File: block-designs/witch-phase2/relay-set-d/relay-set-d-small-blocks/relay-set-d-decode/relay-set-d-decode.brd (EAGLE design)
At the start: 99.1 x 78.7 mm, 85 parts, among them IC1 74LS138D, IC10 74LVC1G32DBV, IC11 74LVC1G32DBV, IC12 74LVC1G32DBV, IC13 74LVC1G125DBV, IC14 74LVC1G125DBV, IC15 74LVC1G125DBV, IC16 74LVC1G125DBV, IC17 74LVC1G125DBV, IC18 74LVC1G125DBV, IC19 74LVC1G125DBV, IC2 74LS138D, IC20 74LVC1G125DBV, IC21 74LVC1G125DBV, IC22 74LVC1G125DBV, IC23 74LVC1G125DBV, IC24 74LVC1G125DBV, IC25 74LVC1G04DBV, IC26 74LVC1G04DBV, IC3 74LS138D, IC4 74LS138D, IC5 74LVC1G32DBV, IC6 74LVC1G32DBV, IC7 74LVC1G32DBV, IC8 74LVC1G32DBV, IC9 74LVC1G32DBV

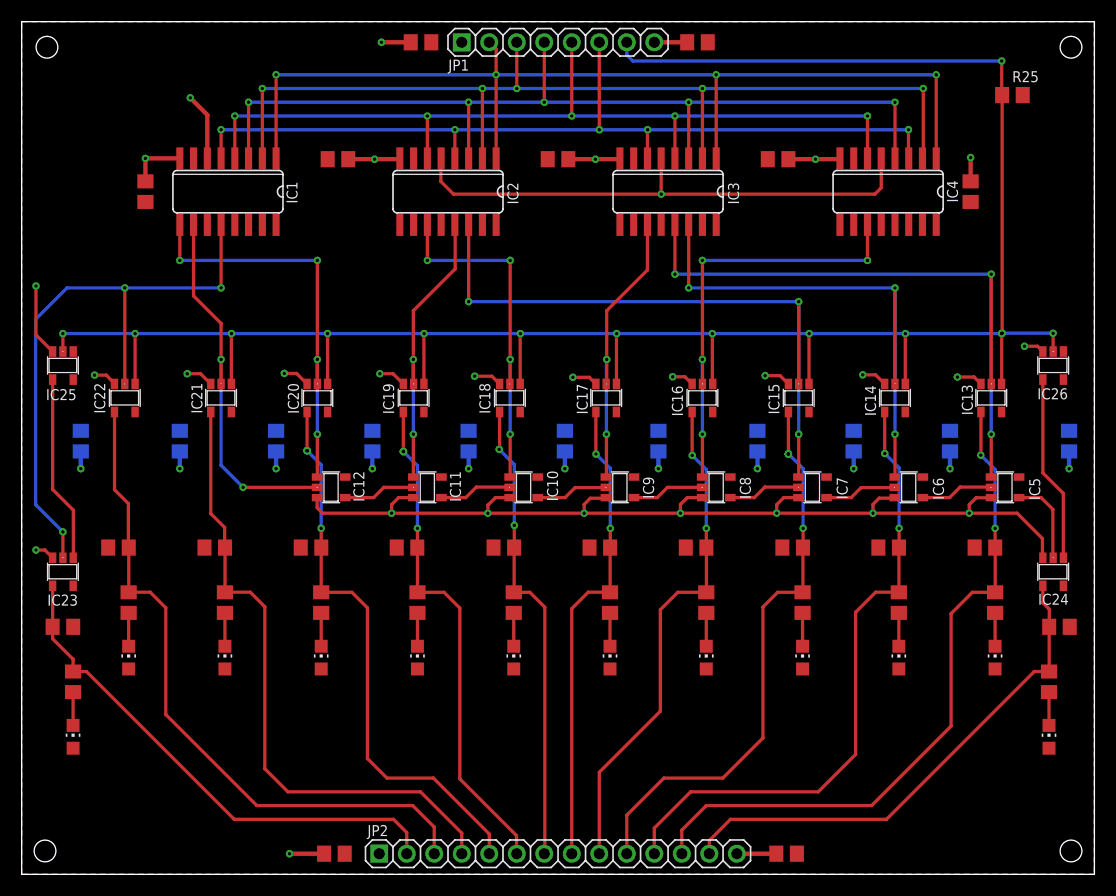
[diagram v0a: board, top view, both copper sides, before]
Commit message: adjust borders for ground/vcc plains and size to match 1.1inch grids
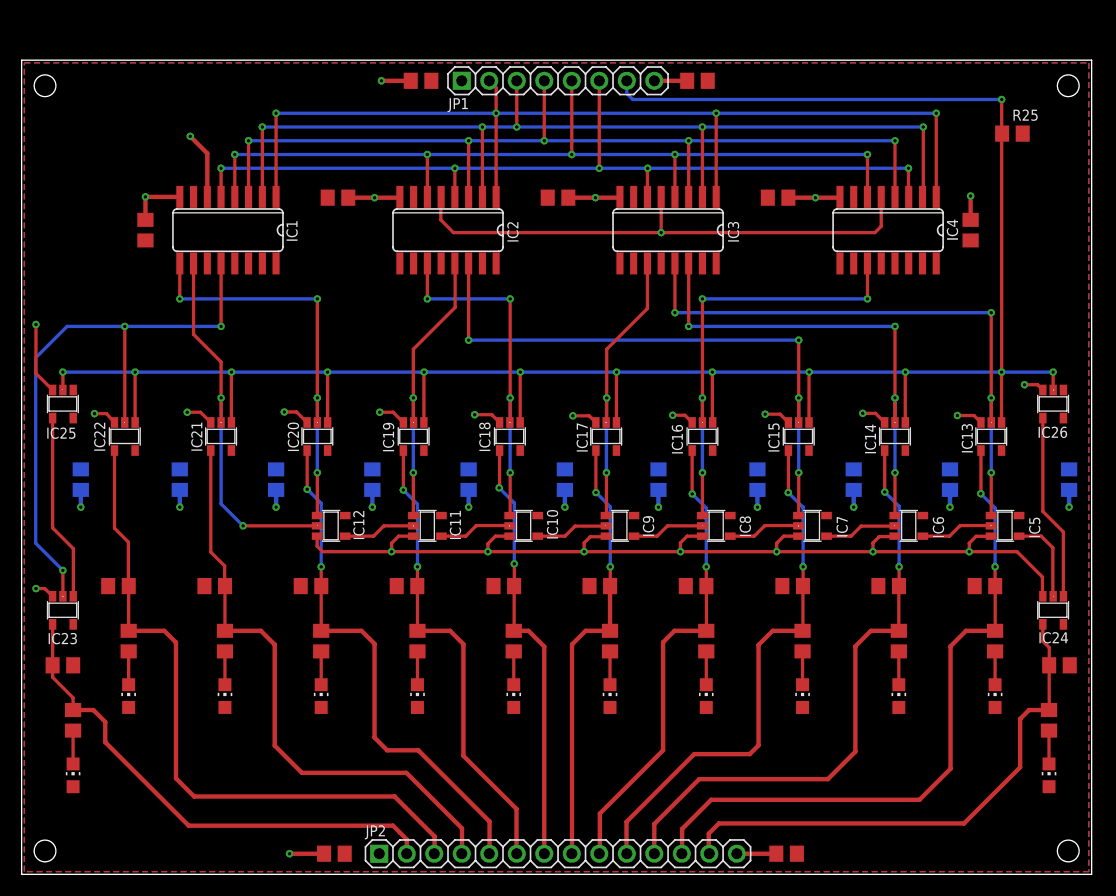
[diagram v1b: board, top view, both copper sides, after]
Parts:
- moved R25 3.56 mm to (91.5, 68.4)
- moved C1 3.56 mm to (29.2, 62.5)
- moved C10 3.56 mm to (67.9, 36.4)
- moved C12 3.56 mm to (76.8, 36.4)
- moved C13 3.56 mm to (5.46, 36.4)
- moved C14 3.56 mm to (85.7, 36.4)
- moved C15 3.56 mm to (14.6, 36.4)
- moved C16 3.56 mm to (96.7, 36.4)
- moved C17 3.56 mm to (23.5, 36.4)
- moved C18 3.56 mm to (32.4, 36.4)
- moved C20 3.56 mm to (41.3, 36.4)
- moved C3 3.56 mm to (49.5, 62.5)
- moved C4 3.56 mm to (69.8, 62.5)
- moved C6 3.56 mm to (50.2, 36.4)
- moved C8 3.56 mm to (58.8, 36.4)
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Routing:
- net NINE: track 62.6 -> 54.8 mm, vias 3 -> 4
- net EIGHT: track 51.2 -> 44.6 mm, vias 3 -> 4
- net SEVEN: track 61.4 -> 56.0 mm, vias 3 -> 4
- net ONE_N: track 58.9 -> 54.5 mm
- net TWO_N: track 52.0 -> 48.1 mm, vias 3 -> 2
- net FOUR_N: track 43.5 -> 39.8 mm
- net SEVEN_N: track 52.6 -> 49.2 mm, vias 3 -> 2
- net FIVE_N: track 44.0 -> 40.6 mm
- net SIX_N: track 47.0 -> 43.6 mm
- net EIGHT_N: track 59.4 -> 56.2 mm
- net THREE_N: track 46.6 -> 43.4 mm, vias 3 -> 2
- net !ONE-NINE_OUT: track 47.2 -> 48.8 mm
- net NINE_N: track 63.5 -> 62.6 mm
- net !ZERO_OUT: track 47.6 -> 46.9 mm
- net DSA-DSB: track 202.7 -> 202.6 mm, vias 14 -> 13
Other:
- board size 99.1 x 78.7 mm -> 98.8 x 75.2 mm

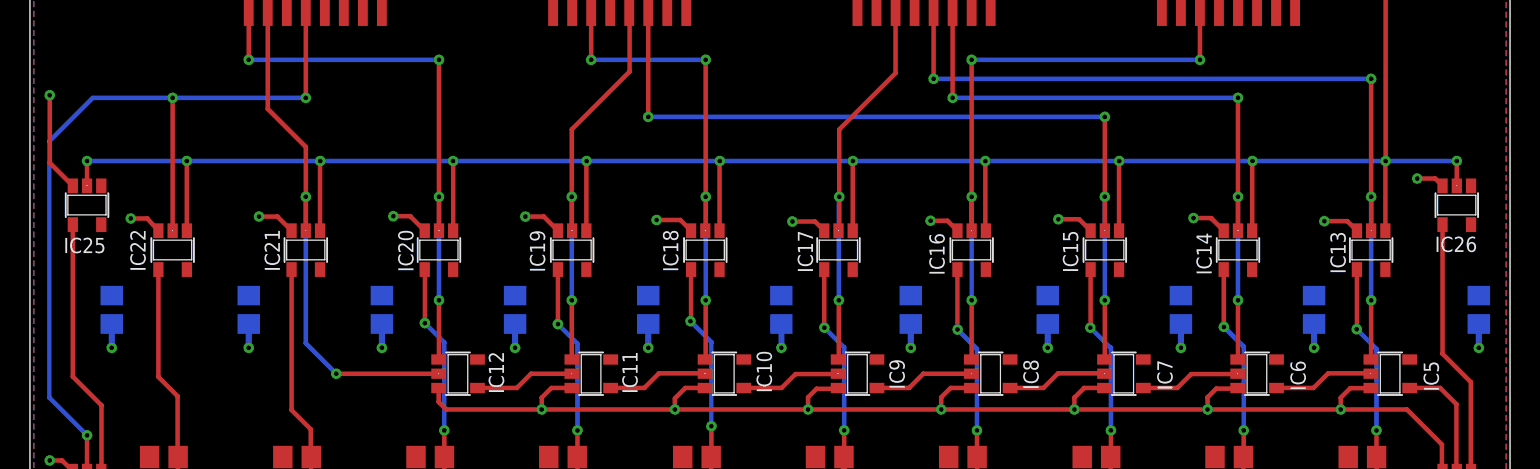
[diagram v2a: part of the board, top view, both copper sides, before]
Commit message: fixes for the decode - change OR gates to AND gates
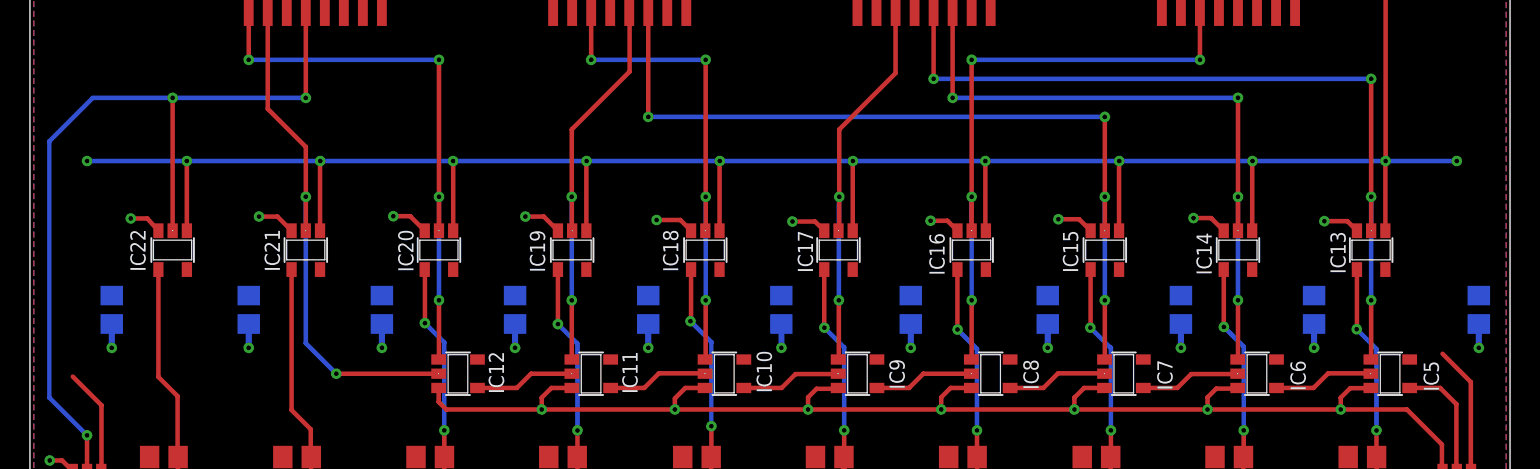
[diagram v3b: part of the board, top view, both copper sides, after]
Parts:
- removed IC25, IC26: 74LVC1G04DBV, 74xx-little-us:SOT23-5
- IC23, IC24: value 74LVC1G125DBV -> 74LVC1G126DBV
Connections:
- net !DSA-DSB-A: no longer IC25.4
- net !DSA-DSB-B: no longer IC26.4
- net DSA-DSB: no longer IC25.2, IC26.2
- net GND: no longer IC25.3, IC26.3
- net VCC: no longer IC25.5, IC26.5
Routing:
- net !DSA-DSB-A: track 17.3 -> 7.11 mm
- net !DSA-DSB-B: track 17.2 -> 8.63 mm
- net GND: track 211.6 -> 203.0 mm, vias 28 -> 26
- net DSA-DSB: track 202.6 -> 199.3 mm
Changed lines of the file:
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@@
 <layer number="43" name="vRestrict" color="2" fill="10" visible="no" active="yes"/>
 <layer number="44" name="Drills" color="7" fill="1" visible="no" active="yes"/>
-<layer number="45" name="Holes" color="7" fill="1" visible="yes" active="yes"/>
+<layer number="45" name="Holes" color="7" fill="1" visible="no" active="yes"/>
 <layer number="46" name="Milling" color="3" fill="1" visible="no" active="yes"/>
 <layer number="47" name="Measures" color="7" fill="1" visible="no" active="yes"/>
 <layer number="48" name="Document" color="7" fill="1" visible="yes" active="yes"/>
-<layer number="49" name="Reference" color="7" fill="1" visible="no" active="yes"/>
+<layer number="49" name="Reference" color="7" fill="1" visible="yes" active="yes"/>
 <layer number="50" name="dxf" color="7" fill="1" visible="no" active="no"/>
 <layer number="51" name="tDocu" color="7" fill="1" visible="yes" active="yes"/>
@@
 <circle x="2.159" y="2.159" radius="2.0066" width="0.0254" layer="41"/>
 <circle x="2.159" y="2.159" radius="2.0066" width="0.0254" layer="42"/>
-<text x="9.2456" y="12.7508" size="1.778" layer="51">0</text>
+<text x="9.2456" y="12.7508" size="1.778" layer="48">0</text>
 <text x="18.161" y="12.7508" size="1.778" layer="51">1</text>
 <text x="27.0002" y="12.7508" size="1.778" layer="51">2</text>
@@
 <text x="80.391" y="12.7508" size="1.778" layer="51">8</text>
 <text x="89.2556" y="12.7508" size="1.778" layer="51">9</text>
-<text x="93.091" y="5.4356" size="1.778" layer="51">1-9</text>
-<text x="4.0386" y="5.4356" size="1.778" layer="51">0</text>
-<text x="8.89" y="2.54" size="1.778" layer="51">Relay Set D
+<text x="93.091" y="5.4356" size="1.778" layer="48">1-9</text>
+<text x="4.0386" y="5.4356" size="1.778" layer="48">0</text>
+<text x="8.89" y="2.54" size="1.778" layer="48">Relay Set D
    Decode </text>
 </plain>
@@
 <attribute name="VALUE" x="89.5858" y="29.1592" size="1.27" layer="27" rot="R180"/>
 </element>
-<element name="IC24" library="74xx-little-us" package="SOT23-5" value="74LVC1G125DBV" x="95.25" y="24.384" smashed="yes" rot="R180">
+<element name="IC24" library="74xx-little-us" package="SOT23-5" value="74LVC1G126DBV" x="95.25" y="24.384" smashed="yes" rot="R180">
 <attribute name="NAME" x="96.6978" y="22.352" size="1.016" layer="25" rot="R180"/>
 </element>
@@
 <attribute name="VALUE" x="9.5758" y="29.1592" size="1.27" layer="27" rot="R180"/>
 </element>
-<element name="IC23" library="74xx-little-us" package="SOT23-5" value="74LVC1G125DBV" x="3.81" y="24.384" smashed="yes" rot="R180">
+<element name="IC23" library="74xx-little-us" package="SOT23-5" value="74LVC1G126DBV" x="3.81" y="24.384" smashed="yes" rot="R180">
 <attribute name="NAME" x="5.207" y="22.2758" size="1.016" layer="25" rot="R180"/>
 </element>
@@
 <element name="R22" library="resistor" package="R0805" value="" x="95.8342" y="19.304" smashed="yes">
 <attribute name="VALUE" x="95.1992" y="16.764" size="1.27" layer="27"/>
-</element>
-<element name="IC25" library="74xx-little-us" package="SOT23-5" value="74LVC1G04DBV" x="3.81" y="43.434" smashed="yes" rot="R180">
-<attribute name="NAME" x="5.08" y="41.2496" size="1.016" layer="25" rot="R180"/>
 </element>
 <element name="LED10" library="led" package="CHIP-LED0805" value="" x="9.8806" y="16.4592" smashed="yes">
@@
 <attribute name="VALUE" x="84.074" y="60.1218" size="1.27" layer="27" ratio="10" rot="R180"/>
 <attribute name="NAME" x="85.4456" y="60.5282" size="1.016" layer="25" ratio="10" rot="R270"/>
-</element>
-<element name="IC26" library="74xx-little-us" package="SOT23-5" value="74LVC1G04DBV" x="95.25" y="43.434" smashed="yes" rot="R180">
-<attribute name="NAME" x="96.6216" y="41.3258" size="1.016" layer="25" rot="R180"/>
 </element>
 <element name="C5" library="resistor" package="C0805" value="" x="36.8808" y="73.279" smashed="yes" rot="R180">
@@
 <contactref element="IC22" pad="3"/>
 <contactref element="IC23" pad="3"/>
-<contactref element="IC25" pad="3"/>
 <contactref element="IC1" pad="8"/>
 <contactref element="IC2" pad="8"/>
@@
 <contactref element="IC4" pad="5"/>
 <contactref element="JP1" pad="8"/>
-<contactref element="IC26" pad="3"/>
 <polygon width="0.254" layer="16">
 <vertex x="98.552" y="0.254"/>
@@
 <wire x1="25.3844" y1="42.6974" x2="24.257" y2="42.6974" width="0.3048" layer="1"/>
 <via x="24.257" y="42.6974" extent="1-16" drill="0.3048"/>
-<wire x1="2.86" y1="44.724" x2="1.3208" y2="46.2632" width="0.3048" layer="1"/>
-<wire x1="1.3208" y1="46.2632" x2="1.3208" y2="50.7746" width="0.3048" layer="1"/>
-<via x="1.3208" y="50.7746" extent="1-16" drill="0.3048"/>
 <wire x1="2.86" y1="25.674" x2="2.1434" y2="26.3906" width="0.3048" layer="1"/>
 <wire x1="2.1434" y1="26.3906" x2="1.3208" y2="26.3906" width="0.3048" layer="1"/>
@@
 <wire x1="87.9446" y1="42.3672" x2="86.4108" y2="42.3672" width="0.3048" layer="1"/>
 <via x="86.4108" y="42.3672" extent="1-16" drill="0.3048"/>
-<wire x1="94.3" y1="44.724" x2="93.812" y2="45.212" width="0.3048" layer="1"/>
-<wire x1="93.812" y1="45.212" x2="92.6084" y2="45.212" width="0.3048" layer="1"/>
-<via x="92.6084" y="45.212" extent="1-16" drill="0.3048"/>
 <wire x1="79.375" y1="62.5602" x2="79.375" y2="59.8424" width="0.3048" layer="1"/>
 <wire x1="79.375" y1="59.8424" x2="78.7908" y2="59.2582" width="0.3048" layer="1"/>
@@
 <contactref element="IC22" pad="5"/>
 <contactref element="IC23" pad="5"/>
-<contactref element="IC25" pad="5"/>
 <contactref element="IC1" pad="16"/>
 <contactref element="IC2" pad="16"/>
@@
 <contactref element="LED12" pad="A"/>
 <wire x1="17.145" y1="66.5734" x2="15.5702" y2="68.1482" width="0.4064" layer="1"/>
-<contactref element="IC26" pad="5"/>
 <polygon width="0.254" layer="1" rank="2">
 <vertex x="98.552" y="0.254"/>
@@
 <contactref element="IC21" pad="1"/>
 <contactref element="IC22" pad="1"/>
-<contactref element="IC25" pad="2"/>
 <wire x1="10.475" y1="41.7268" x2="10.475" y2="46.3804" width="0.3048" layer="1"/>
 <wire x1="10.475" y1="46.3804" x2="19.3802" y2="46.3804" width="0.3048" layer="16"/>
@@
 <wire x1="56.4388" y1="71.5518" x2="55.88" y2="72.1106" width="0.3048" layer="16"/>
 <wire x1="55.88" y1="72.1106" x2="55.88" y2="73.279" width="0.3048" layer="16"/>
-<contactref element="IC26" pad="2"/>
 <wire x1="10.475" y1="46.3804" x2="3.81" y2="46.3804" width="0.3048" layer="16"/>
 <via x="3.81" y="46.3804" extent="1-16" drill="0.3048"/>
-<wire x1="3.81" y1="46.3804" x2="3.81" y2="44.724" width="0.3048" layer="1"/>
 <via x="95.25" y="46.3804" extent="1-16" drill="0.3048"/>
 <wire x1="90.5002" y1="46.3804" x2="95.25" y2="46.3804" width="0.3048" layer="16"/>
-<wire x1="95.25" y1="44.724" x2="95.25" y2="46.3804" width="0.3048" layer="1"/>
 <wire x1="81.6102" y1="46.3804" x2="90.5002" y2="46.3804" width="0.3048" layer="16"/>
 <wire x1="90.485" y1="41.7268" x2="90.485" y2="46.3652" width="0.3048" layer="1"/>
@@
 <signal name="!DSA-DSB-A">
 <contactref element="IC23" pad="1"/>
-<contactref element="IC25" pad="4"/>
-<wire x1="2.86" y1="42.134" x2="2.86" y2="31.9888" width="0.3048" layer="1"/>
 <wire x1="2.86" y1="31.9888" x2="4.7752" y2="30.0736" width="0.3048" layer="1"/>
 <wire x1="4.7752" y1="30.0736" x2="4.7752" y2="25.6892" width="0.3048" layer="1"/>
@@
 </signal>
 <signal name="!DSA-DSB-B">
-<contactref element="IC26" pad="4"/>
 <contactref element="IC24" pad="1"/>
-<wire x1="94.3" y1="42.134" x2="94.3" y2="33.5128" width="0.3048" layer="1"/>
 <wire x1="94.3" y1="33.5128" x2="96.1898" y2="31.623" width="0.3048" layer="1"/>
 <wire x1="96.1898" y1="31.623" x2="96.1898" y2="25.6842" width="0.3048" layer="1"/>

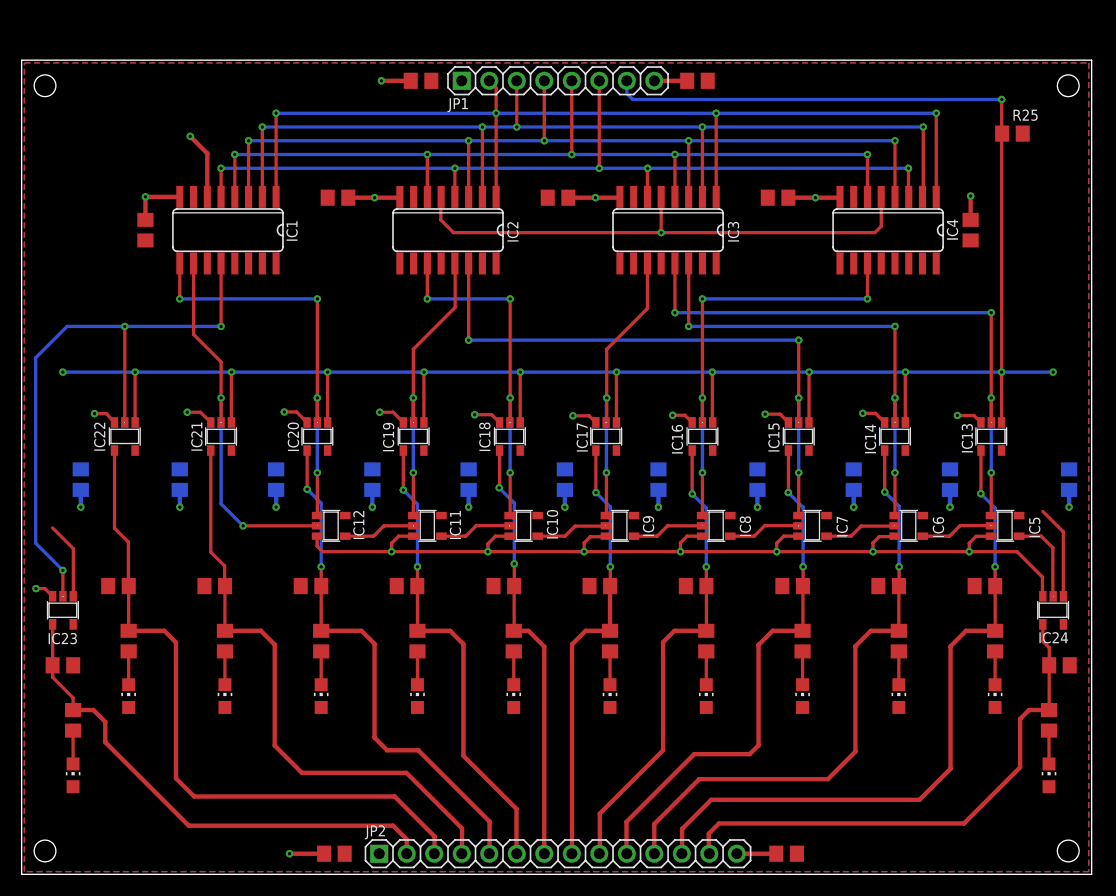
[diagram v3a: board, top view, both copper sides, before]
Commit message: remove 0 and 1-9 special decodes for basic testing
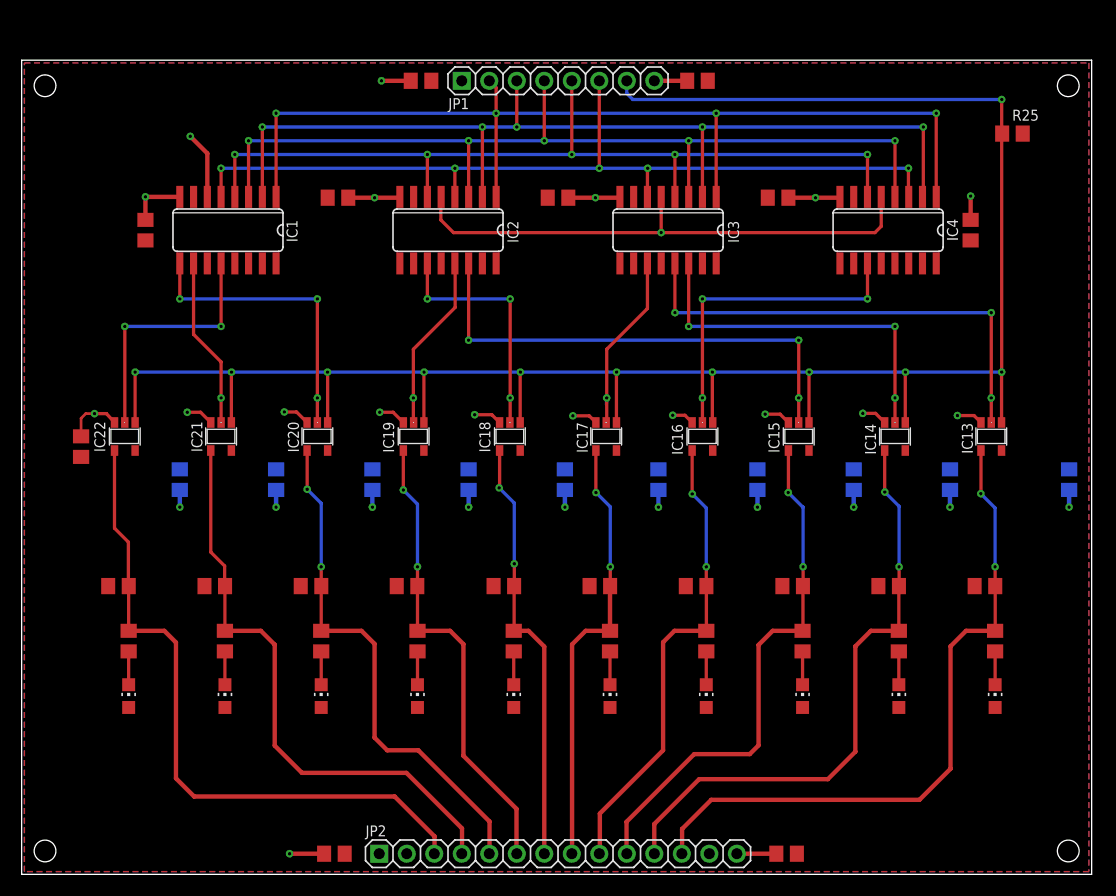
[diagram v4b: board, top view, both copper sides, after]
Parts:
- removed IC10, IC11, IC12, IC5, IC6, IC7, IC8, IC9: 74LVC1G32DBV, 74xx-little-us:SOT23-5
- removed IC23, IC24: 74LVC1G126DBV, 74xx-little-us:SOT23-5
- removed LED11, LED12: (no value), led:CHIP-LED0805
- removed R21, R22, R23, R24: (no value), resistor:R0805
- moved C13 3.05 mm to (5.49, 39.5), flipped to the top
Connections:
- removed net !DSA-DSB-A: IC23.1
- removed net !DSA-DSB-B: IC24.1
- removed net N$11: IC8.2, IC9.4
- removed net N$12: IC10.4, IC9.2
- removed net N$13: IC10.2, IC11.4
- removed net N$14: IC11.2, IC12.4
- removed net N$15: LED11.C, R23.2
- removed net N$17: IC5.2, IC6.4
- removed net N$18: IC6.2, IC7.4
- removed net N$19: IC7.2, IC8.4
- removed net N$20: LED12.C, R24.2
- removed net ONE-NINE: IC24.2, IC5.4
- net !ONE-NINE_OUT: no longer IC24.4, R22.1, R24.1
- net !ZERO_OUT: no longer IC23.4, R21.1, R23.1
- net EIGHT: no longer IC6.1
- net FIVE: no longer IC9.1
- net FOUR: no longer IC10.1
- net GND: no longer IC10.3, IC11.3, IC12.3, IC23.3, IC24.3, IC5.3, IC6.3, IC7.3, IC8.3, IC9.3
- net NINE: no longer IC5.1
- net ONE: no longer IC12.2
- net SEVEN: no longer IC7.1
- net SIX: no longer IC8.1
- net THREE: no longer IC11.1
- net TWO: no longer IC12.1
- net VCC: no longer IC10.5, IC11.5, IC12.5, IC23.5, IC24.5, IC5.5, IC6.5, IC7.5, IC8.5, IC9.5, LED11.A, LED12.A, R21.2, R22.2
- net ZERO: no longer IC23.2
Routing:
- net GND: track 203.0 -> 111.6 mm, vias 26 -> 18
- net !ONE-NINE_OUT: track 48.8 -> 0.00 mm
- net !ZERO_OUT: track 46.9 -> 0.00 mm
- net ZERO: track 56.1 -> 23.6 mm, vias 3 -> 2
- net ONE: track 35.2 -> 15.7 mm, vias 2 -> 1
- net DSA-DSB: track 199.3 -> 187.9 mm, vias 13 -> 11
- net FOUR: track 33.2 -> 22.4 mm, vias 4 -> 3
- net SIX: track 40.8 -> 29.9 mm, vias 4 -> 3
- net SEVEN: track 56.0 -> 45.2 mm, vias 4 -> 3
- net NINE: track 54.8 -> 43.9 mm, vias 4 -> 3
- net EIGHT: track 44.6 -> 33.7 mm, vias 4 -> 3
- net TWO: track 38.3 -> 27.4 mm, vias 4 -> 3
- net THREE: track 27.2 -> 16.3 mm, vias 2 -> 1
- net FIVE: track 27.2 -> 16.9 mm, vias 2 -> 1
- net !DSA-DSB-B: track 8.63 -> 0.00 mm
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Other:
- board text removed: "1-9"
